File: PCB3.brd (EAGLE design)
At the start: 100 x 80 mm, 52 parts

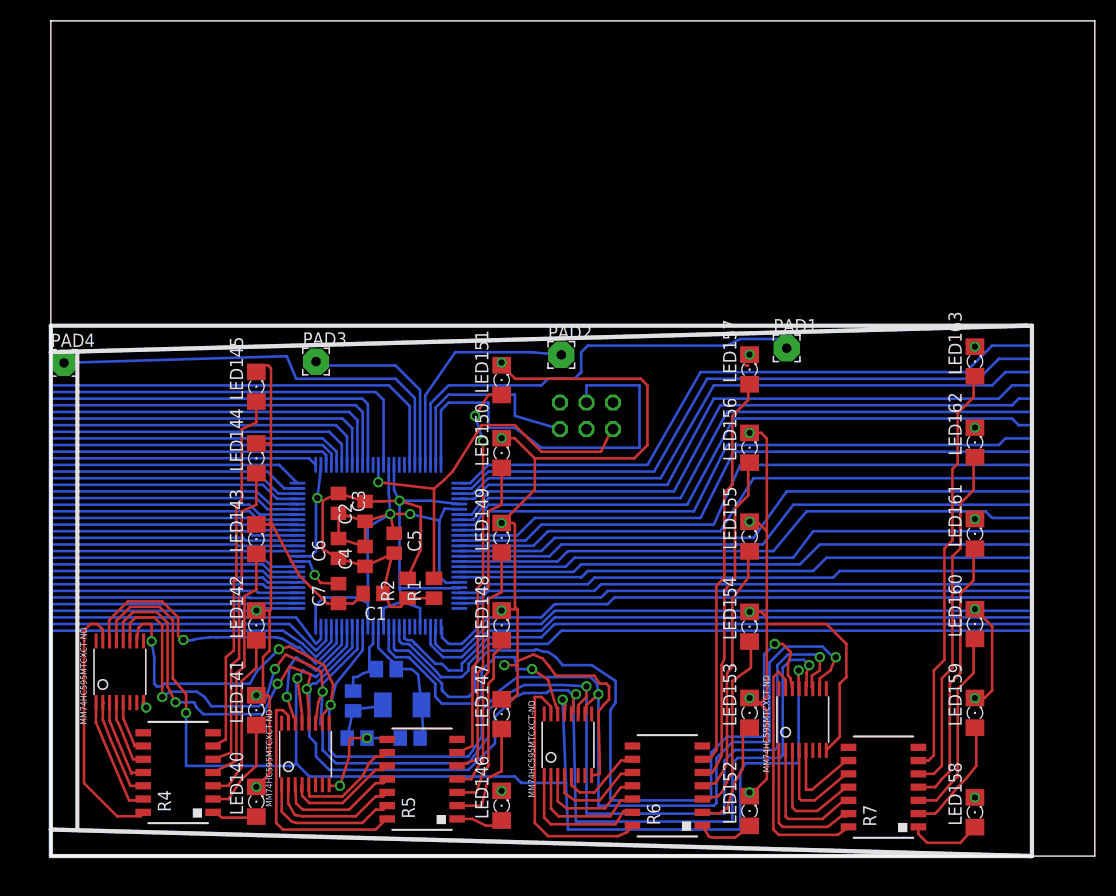
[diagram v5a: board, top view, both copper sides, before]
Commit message: Finished PCB1, PCB3, and added parts to ECE477 library
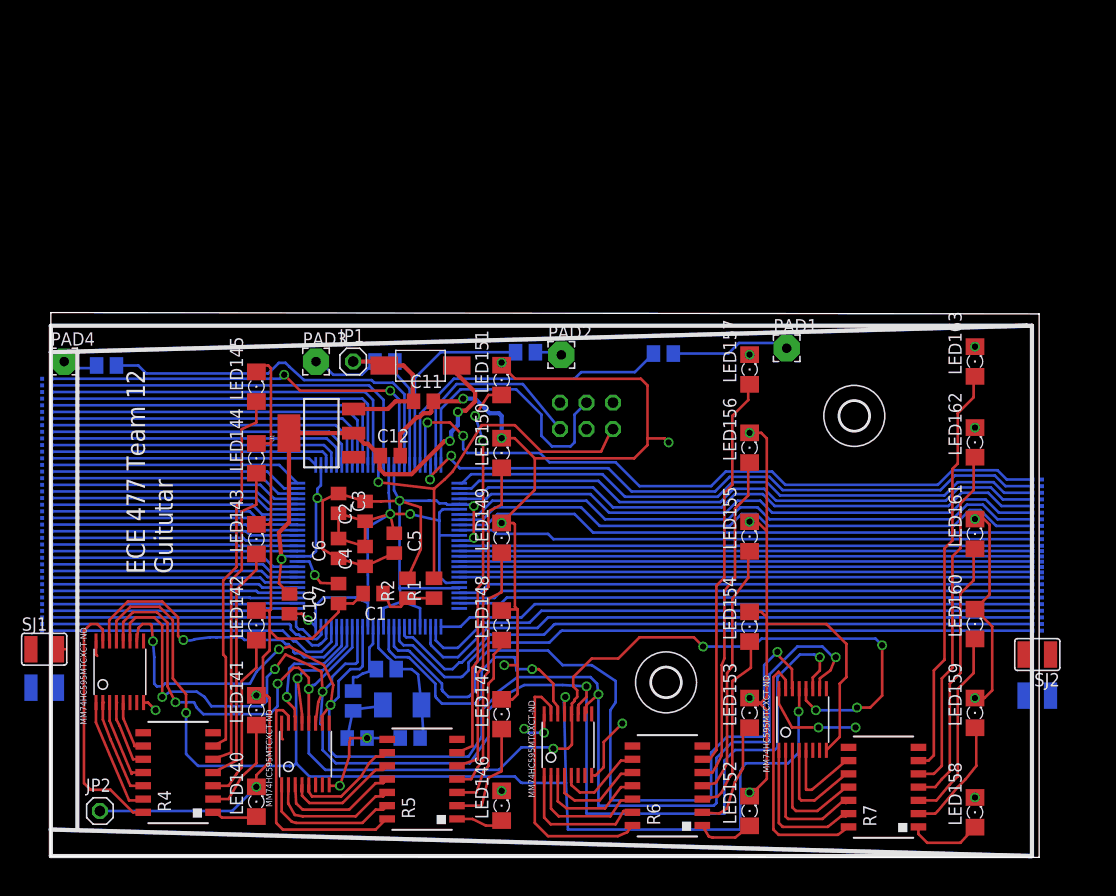
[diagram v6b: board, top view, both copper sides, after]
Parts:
- added C10: (no value), rcl:C0805
- added C11: 10uF, rcl:C0805
- added C12: 100uF, rcl:C0805
- added D1: S1BFSCT, ECE477_Guitutar:S1BFSCT
- added H1, H2: MOUNT-HOLE2.8, holes:2,8
- added JP1, JP2: (no value), pinhead:1X01
- added R10, R11, R12, R9: 330k, rcl:M0805
- added SJ1, SJ2, SJ3, SJ4: (no value), jumper:SJW
- added U$1, U$10, U$11, U$12, U$13, U$14, U$15, U$16, U$17, U$18, U$19, U$20, U$21, U$22, U$23, U$24, U$25, U$3, U$30, U$31, U$32, U$33, U$34, U$35, U$36, U$37, U$38, U$39, U$4, U$40, U$41, U$42, U$43, U$44, U$45, U$46, U$47, U$48, U$49, U$5, U$50, U$51, U$52, U$53, U$54, U$55, U$56, U$57, U$58, U$59, U$6, U$60, U$61, U$62, U$63, U$64, U$65, U$66, U$67, U$68, U$69, U$7, U$8, U$9: JUMPER, ECE477_Guitutar:JUMPER
- added U1: (no value), SparkFun-IC-Power:SOT223
- moved PAD4 0.13 mm to (1.27, 47.4)
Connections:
- new net 5.2V_PB: C11.1, D1.P$1, JP1.1, U1.3
- new net N$3: PAD1.1, R12.2
- new net N$4: PAD2.1, R11.2
- new net N$5: PAD3.1, R10.2
- new net N$7: PAD4.1, R9.2
- net FRET10: now also U$2.22; no longer U$2.26
- net FRET11: now also U$2.23; no longer U$2.27
- net FRET12: now also U$2.26; no longer U$2.28
- net FRET13: now also U$2.27; no longer U$2.29
- net FRET14: now also U$2.28; no longer U$2.32
- net FRET15: now also U$2.29; no longer U$2.33
- net FRET16: now also U$2.32; no longer U$2.34
- net FRET17: now also U$2.33; no longer U$2.35
- net FRET18: now also U$2.34; no longer U$2.36
- net FRET19: now also U$2.35; no longer U$2.37
- net FRET5: now also U$2.17; no longer U$2.19
- net FRET6: now also R9.1, U$2.18; no longer PAD4.1, U$2.20
- net FRET7: now also R10.1, U$2.19; no longer PAD3.1, U$2.21
- net FRET8: now also R11.1, U$2.20; no longer PAD2.1, U$2.22
- net FRET9: now also R12.1, U$2.21; no longer PAD1.1, U$2.23
- net GND: now also C11.2, C12.2, JP2.1, SJ3.1, SJ3.2, SJ4.1, SJ4.2
- net VDD: now also C10.1, C12.1, D1.P$2, SJ1.1, SJ1.2, SJ2.1, SJ2.2, U$2.37, U1.2, U1.4
- net VSS: now also C10.2, U$2.36
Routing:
- net VDD: track 72.0 -> 125.8 mm, vias 2 -> 7
- net TXD: track 0.00 -> 37.4 mm
- net GND: track 231.2 -> 261.7 mm, vias 24 -> 23
- net 5.2V_PB: track 0.00 -> 14.8 mm
- net FRET9: track 43.9 -> 29.7 mm
- net N$14: track 40.3 -> 26.8 mm
- net N$3: track 0.00 -> 11.5 mm
- net N$124: track 0.00 -> 10.1 mm, vias 0 -> 2
- net FRET7: track 18.3 -> 10.5 mm
- net N$5: track 0.00 -> 6.71 mm
- net FRET6: track 42.2 -> 36.3 mm
- net RCK: track 135.8 -> 130.0 mm, vias 5 -> 8
- net FRET10: track 61.8 -> 67.4 mm, vias 0 -> 2
- net VSS: track 53.7 -> 58.8 mm, vias 2 -> 3
- net G: track 135.0 -> 130.3 mm
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- added copper zone on layer 1, net VDD
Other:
- board size 100 x 80 mm -> 94.7 x 52.2 mm
- board text added: "ECE 477 Team 12 Guitutar"

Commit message: Added pin AMP to micro for amplifier circuit
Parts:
- added U$70: JUMPER, ECE477_Guitutar:JUMPER
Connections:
- new net AMP: U$2.50
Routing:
- net AMP: track 0.00 -> 61.1 mm, vias 0 -> 4
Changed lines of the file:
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@@
 <element name="R11" library="rcl" package="M0805" value="330k" x="45.466" y="48.26" rot="MR180"/>
 <element name="R12" library="rcl" package="M0805" value="330k" x="58.674" y="48.133" rot="MR180"/>
+<element name="U$70" library="ECE477_Guitutar" package="JUMPER" value="JUMPER" x="94.488" y="36.703" rot="MR0"/>
 </elements>
 <signals>
@@
 <wire x1="29.911" y1="25.146" x2="28.961" y2="24.196" width="0.254" layer="1"/>
 <wire x1="28.961" y1="24.196" x2="27.559" y2="24.196" width="0.254" layer="1"/>
-<wire x1="43.18" y1="23.52" x2="43.282" y2="23.622" width="0.254" layer="1"/>
-<wire x1="44.704" y1="23.622" x2="43.282" y2="23.622" width="0.254" layer="1"/>
-<wire x1="44.704" y1="18.288" x2="44.704" y2="23.622" width="0.254" layer="1"/>
+<wire x1="43.282" y1="23.622" x2="43.18" y2="23.52" width="0.254" layer="1"/>
+<wire x1="44.704" y1="22.733" x2="44.704" y2="18.288" width="0.254" layer="1"/>
 <wire x1="44.704" y1="18.288" x2="44.704" y2="15.494" width="0.254" layer="1"/>
 <wire x1="44.704" y1="15.494" x2="44.221" y2="15.011" width="0.254" layer="1"/>
@@
 <wire x1="43.18" y1="31.902" x2="44.298" y2="31.902" width="0.254" layer="1"/>
 <wire x1="44.298" y1="31.902" x2="44.45" y2="31.75" width="0.254" layer="1"/>
-<wire x1="44.45" y1="31.75" x2="44.45" y2="23.876" width="0.254" layer="1"/>
-<wire x1="44.45" y1="23.876" x2="44.704" y2="23.622" width="0.254" layer="1"/>
+<wire x1="44.45" y1="23.622" x2="44.45" y2="31.75" width="0.254" layer="1"/>
+<wire x1="44.45" y1="23.622" x2="44.45" y2="22.987" width="0.254" layer="1"/>
 <wire x1="88.519" y1="23.647" x2="90.17" y2="21.996" width="0.254" layer="1"/>
 <wire x1="90.17" y1="21.996" x2="90.17" y2="15.875" width="0.254" layer="1"/>
@@
 <wire x1="52.959" y1="10.922" x2="54.737" y2="12.7" width="0.254" layer="1"/>
 <via x="54.737" y="12.7" extent="1-16" drill="0.6"/>
-<wire x1="93.218" y1="15.367" x2="95.758" y2="15.367" width="0" layer="19" extent="16-16"/>
+<wire x1="44.45" y1="22.987" x2="44.704" y2="22.733" width="0.254" layer="1"/>
+<wire x1="43.18" y1="23.52" x2="44.348" y2="23.52" width="0.254" layer="1"/>
+<wire x1="44.348" y1="23.52" x2="44.45" y2="23.622" width="0.254" layer="1"/>
+<wire x1="88.519" y1="41.046" x2="88.519" y2="48.793" width="0" layer="19" extent="1-1"/>
+<wire x1="88.519" y1="32.283" x2="88.519" y2="41.046" width="0" layer="19" extent="1-1"/>
+<wire x1="93.218" y1="15.367" x2="90.17" y2="15.875" width="0" layer="19" extent="1-16"/>
+<wire x1="95.758" y1="15.367" x2="93.218" y2="15.367" width="0" layer="19" extent="16-16"/>
+<wire x1="88.519" y1="5.613" x2="88.519" y2="15.138" width="0" layer="19" extent="1-1"/>
+<wire x1="76.2" y1="17.145" x2="88.519" y2="15.138" width="0" layer="19" extent="1-1"/>
+<wire x1="66.929" y1="48.031" x2="66.929" y2="40.538" width="0" layer="19" extent="1-1"/>
+<wire x1="59.182" y1="39.624" x2="66.929" y2="40.538" width="0" layer="19" extent="1-1"/>
+<wire x1="57.15" y1="39.37" x2="57.15" y2="40.005" width="0" layer="19" extent="1-1"/>
 <wire x1="43.18" y1="47.269" x2="43.18" y2="47.015" width="0" layer="19" extent="1-1"/>
+<wire x1="43.18" y1="6.248" x2="43.18" y2="15.011" width="0" layer="19" extent="1-1"/>
+<wire x1="51.805" y1="7.718" x2="43.18" y2="6.248" width="0" layer="19" extent="1-1"/>
+<wire x1="33.467" y1="11.303" x2="43.18" y2="15.011" width="0" layer="19" extent="1-16"/>
+<wire x1="20.955" y1="9.017" x2="26.659" y2="6.829" width="0" layer="19" extent="1-1"/>
+<wire x1="10.033" y1="13.97" x2="19.685" y2="15.392" width="0" layer="19" extent="1-1"/>
+<wire x1="0.635" y1="16.129" x2="8.879" y2="14.703" width="0" layer="19" extent="1-16"/>
 <wire x1="-1.905" y1="16.129" x2="0.635" y2="16.129" width="0" layer="19" extent="16-16"/>
 </signal>
@@
 <wire x1="37.369" y1="21.968" x2="39.24" y2="21.968" width="0.254" layer="16"/>
 <wire x1="39.24" y1="21.968" x2="40.132" y2="22.86" width="0.254" layer="16"/>
-<wire x1="40.132" y1="22.86" x2="45.085" y2="22.86" width="0.254" layer="16"/>
-<wire x1="45.085" y1="22.86" x2="46.355" y2="24.13" width="0.254" layer="16"/>
-<wire x1="46.355" y1="24.13" x2="93.98" y2="24.13" width="0.254" layer="16"/>
+<wire x1="40.132" y1="22.86" x2="45.466" y2="22.86" width="0.254" layer="16"/>
+<wire x1="45.466" y1="22.86" x2="46.736" y2="24.13" width="0.254" layer="16"/>
+<wire x1="46.736" y1="24.13" x2="93.98" y2="24.13" width="0.254" layer="16"/>
 </signal>
 <signal name="LED_SER15">
@@
 <wire x1="4.13" y1="46.736" x2="4.384" y2="46.99" width="0.254" layer="16"/>
 </signal>
+<signal name="AMP">
+<contactref element="U$2" pad="50"/>
+<wire x1="39.119" y1="23.718" x2="45.054" y2="23.718" width="0.254" layer="16"/>
+<wire x1="45.054" y1="23.718" x2="45.339" y2="24.003" width="0.254" layer="16"/>
+<via x="45.339" y="24.003" extent="1-16" drill="0.6"/>
+<wire x1="45.339" y1="24.003" x2="49.784" y2="24.003" width="0.254" layer="1"/>
+<wire x1="49.784" y1="24.003" x2="63.246" y2="37.465" width="0.254" layer="1"/>
+<wire x1="63.246" y1="37.465" x2="63.373" y2="37.465" width="0.254" layer="1"/>
+<wire x1="63.373" y1="37.465" x2="63.5" y2="37.592" width="0.254" layer="1"/>
+<via x="63.5" y="37.592" extent="1-16" drill="0.6"/>
+<wire x1="63.5" y1="37.592" x2="70.739" y2="37.592" width="0.254" layer="16"/>
+<wire x1="70.739" y1="37.592" x2="70.866" y2="37.465" width="0.254" layer="16"/>
+<via x="70.866" y="37.465" extent="1-16" drill="0.6"/>
+<wire x1="70.866" y1="37.465" x2="83.947" y2="37.465" width="0.254" layer="1"/>
+<wire x1="83.947" y1="37.465" x2="84.074" y2="37.592" width="0.254" layer="1"/>
+<via x="84.074" y="37.592" extent="1-16" drill="0.6"/>
+<wire x1="84.074" y1="37.592" x2="90.805" y2="37.592" width="0.254" layer="16"/>
+<wire x1="90.805" y1="37.592" x2="91.694" y2="36.703" width="0.254" layer="16"/>
+<wire x1="91.694" y1="36.703" x2="93.98" y2="36.703" width="0.254" layer="16"/>
+</signal>
 </signals>
